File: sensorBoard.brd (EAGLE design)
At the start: 20 x 50 mm, 34 parts, among them Q1 BSS84, U1 ADXL345, U2 L3G4200D, U3 MPL115A, X1 22-23-2051

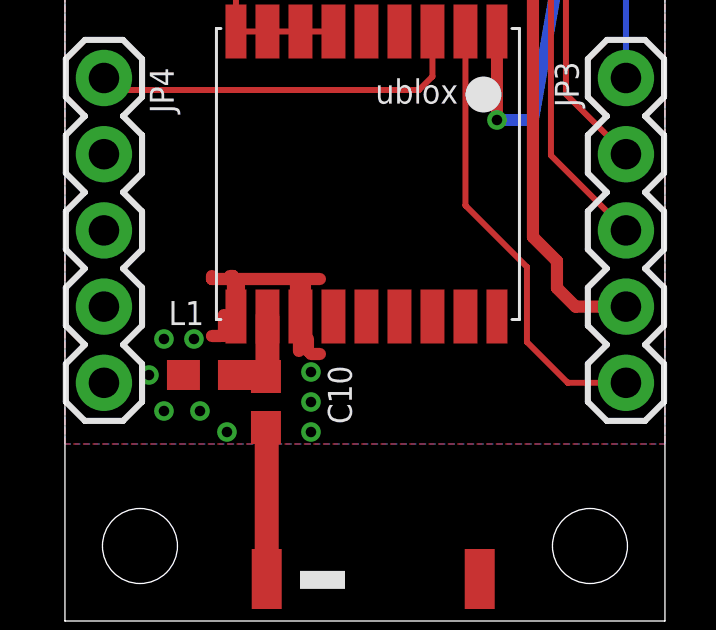
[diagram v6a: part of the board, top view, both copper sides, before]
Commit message: Fixed ground issue
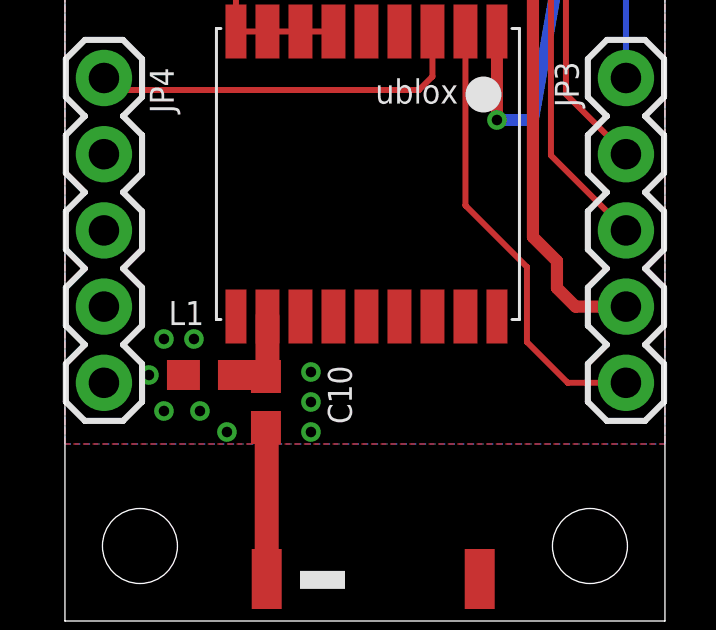
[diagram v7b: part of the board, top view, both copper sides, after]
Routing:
- net N$16: track 3.70 -> 0.00 mm
- net N$13: track 1.20 -> 0.00 mm
- net N$10: track 1.00 -> 0.00 mm
- net N$14: track 0.70 -> 0.00 mm
- net N$11: track 0.60 -> 0.00 mm
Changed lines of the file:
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@@
 <?xml version="1.0" encoding="utf-8"?>
 <!DOCTYPE eagle SYSTEM "eagle.dtd">
-<eagle version="7.3.0">
+<eagle version="7.2.0">
 <drawing>
 <settings>
@@
 <layer number="21" name="tPlace" color="7" fill="1" visible="yes" active="yes"/>
 <layer number="22" name="bPlace" color="7" fill="1" visible="yes" active="yes"/>
-<layer number="23" name="tOrigins" color="15" fill="1" visible="yes" active="yes"/>
-<layer number="24" name="bOrigins" color="15" fill="1" visible="yes" active="yes"/>
+<layer number="23" name="tOrigins" color="15" fill="1" visible="no" active="yes"/>
+<layer number="24" name="bOrigins" color="15" fill="1" visible="no" active="yes"/>
 <layer number="25" name="tNames" color="7" fill="1" visible="yes" active="yes"/>
 <layer number="26" name="bNames" color="7" fill="1" visible="yes" active="yes"/>
-<layer number="27" name="tValues" color="7" fill="1" visible="yes" active="yes"/>
-<layer number="28" name="bValues" color="7" fill="1" visible="yes" active="yes"/>
-<layer number="29" name="tStop" color="7" fill="3" visible="yes" active="yes"/>
-<layer number="30" name="bStop" color="7" fill="6" visible="yes" active="yes"/>
-<layer number="31" name="tCream" color="7" fill="4" visible="yes" active="yes"/>
-<layer number="32" name="bCream" color="7" fill="5" visible="yes" active="yes"/>
+<layer number="27" name="tValues" color="7" fill="1" visible="no" active="yes"/>
+<layer number="28" name="bValues" color="7" fill="1" visible="no" active="yes"/>
+<layer number="29" name="tStop" color="7" fill="3" visible="no" active="yes"/>
+<layer number="30" name="bStop" color="7" fill="6" visible="no" active="yes"/>
+<layer number="31" name="tCream" color="7" fill="4" visible="no" active="yes"/>
+<layer number="32" name="bCream" color="7" fill="5" visible="no" active="yes"/>
 <layer number="33" name="tFinish" color="6" fill="3" visible="yes" active="yes"/>
 <layer number="34" name="bFinish" color="6" fill="6" visible="yes" active="yes"/>
@@
 <contactref element="U2" pad="8"/>
 <contactref element="R1" pad="1"/>
-<wire x1="8.2" y1="8.3" x2="7.85" y2="10.15" width="0" layer="19" extent="1-1"/>
-<wire x1="5.7" y1="10.15" x2="4.3" y2="9.4" width="0" layer="19" extent="1-1"/>
 </signal>
 <signal name="VBAT">
@@
 </signal>
 <signal name="N$10">
-<wire x1="7.7" y1="11.4" x2="7.7" y2="11" width="0.4064" layer="1"/>
-<wire x1="7.7" y1="11" x2="8" y2="11" width="0.4064" layer="1"/>
-<wire x1="8" y1="11" x2="8" y2="11.3" width="0.4064" layer="1"/>
 </signal>
 <signal name="N$11">
-<wire x1="7.7" y1="9.5" x2="7.8" y2="9.5" width="0.4064" layer="1"/>
-<wire x1="7.8" y1="9.5" x2="7.8" y2="9" width="0.4064" layer="1"/>
 </signal>
 <signal name="N$12">
-<wire x1="8.1" y1="9.4" x2="8.1" y2="9" width="0.4064" layer="1"/>
 </signal>
 <signal name="N$13">
-<wire x1="5.5" y1="11.5" x2="5.6" y2="11.5" width="0.4064" layer="1"/>
-<wire x1="5.6" y1="11.5" x2="5.6" y2="11" width="0.4064" layer="1"/>
-<wire x1="5.6" y1="11" x2="5.8" y2="11" width="0.4064" layer="1"/>
-<wire x1="5.8" y1="11" x2="5.8" y2="11.4" width="0.4064" layer="1"/>
-</signal>
-<signal name="N$14">
-<wire x1="5.3" y1="10.2" x2="5.3" y2="9.5" width="0.4064" layer="1"/>
-</signal>
-<signal name="N$15">
-<wire x1="4.9" y1="9.5" x2="5.2" y2="9.5" width="0.4064" layer="1"/>
-</signal>
-<signal name="N$16">
-<wire x1="4.9" y1="11.5" x2="4.9" y2="11.4" width="0.4064" layer="1"/>
-<wire x1="4.9" y1="11.4" x2="8.5" y2="11.4" width="0.4064" layer="1"/>
 </signal>
 <signal name="N$17">
-<wire x1="8.2" y1="8.9" x2="8.5" y2="8.9" width="0.4064" layer="1"/>
 </signal>
 </signals>

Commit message: Added EARS Logo
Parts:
- added U$10: EARS-LOGO, earsLogo:EARS-LOGO
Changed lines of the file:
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@@
 <layer number="21" name="tPlace" color="7" fill="1" visible="yes" active="yes"/>
 <layer number="22" name="bPlace" color="7" fill="1" visible="yes" active="yes"/>
-<layer number="23" name="tOrigins" color="15" fill="1" visible="no" active="yes"/>
-<layer number="24" name="bOrigins" color="15" fill="1" visible="no" active="yes"/>
+<layer number="23" name="tOrigins" color="15" fill="1" visible="yes" active="yes"/>
+<layer number="24" name="bOrigins" color="15" fill="1" visible="yes" active="yes"/>
 <layer number="25" name="tNames" color="7" fill="1" visible="yes" active="yes"/>
 <layer number="26" name="bNames" color="7" fill="1" visible="yes" active="yes"/>
@@
 <attribute name="VALUE" x="18.005" y="35.765" size="0.8" layer="27" rot="R90"/>
 </element>
+<element name="U$10" library="earsLogo" package="EARS-LOGO" value="EARS-LOGO" x="9.4" y="32.7" rot="MR0"/>
 </elements>
 <signals>
